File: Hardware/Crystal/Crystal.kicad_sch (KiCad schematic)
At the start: 48 parts, among them J1 USB_B_Micro, U1 AP63205WU, U2 NCP1117-3.3_SOT223, U3 ESP32-C3-WROOM-02, U4 TXS0102DCT, U5 TXS0108EPW

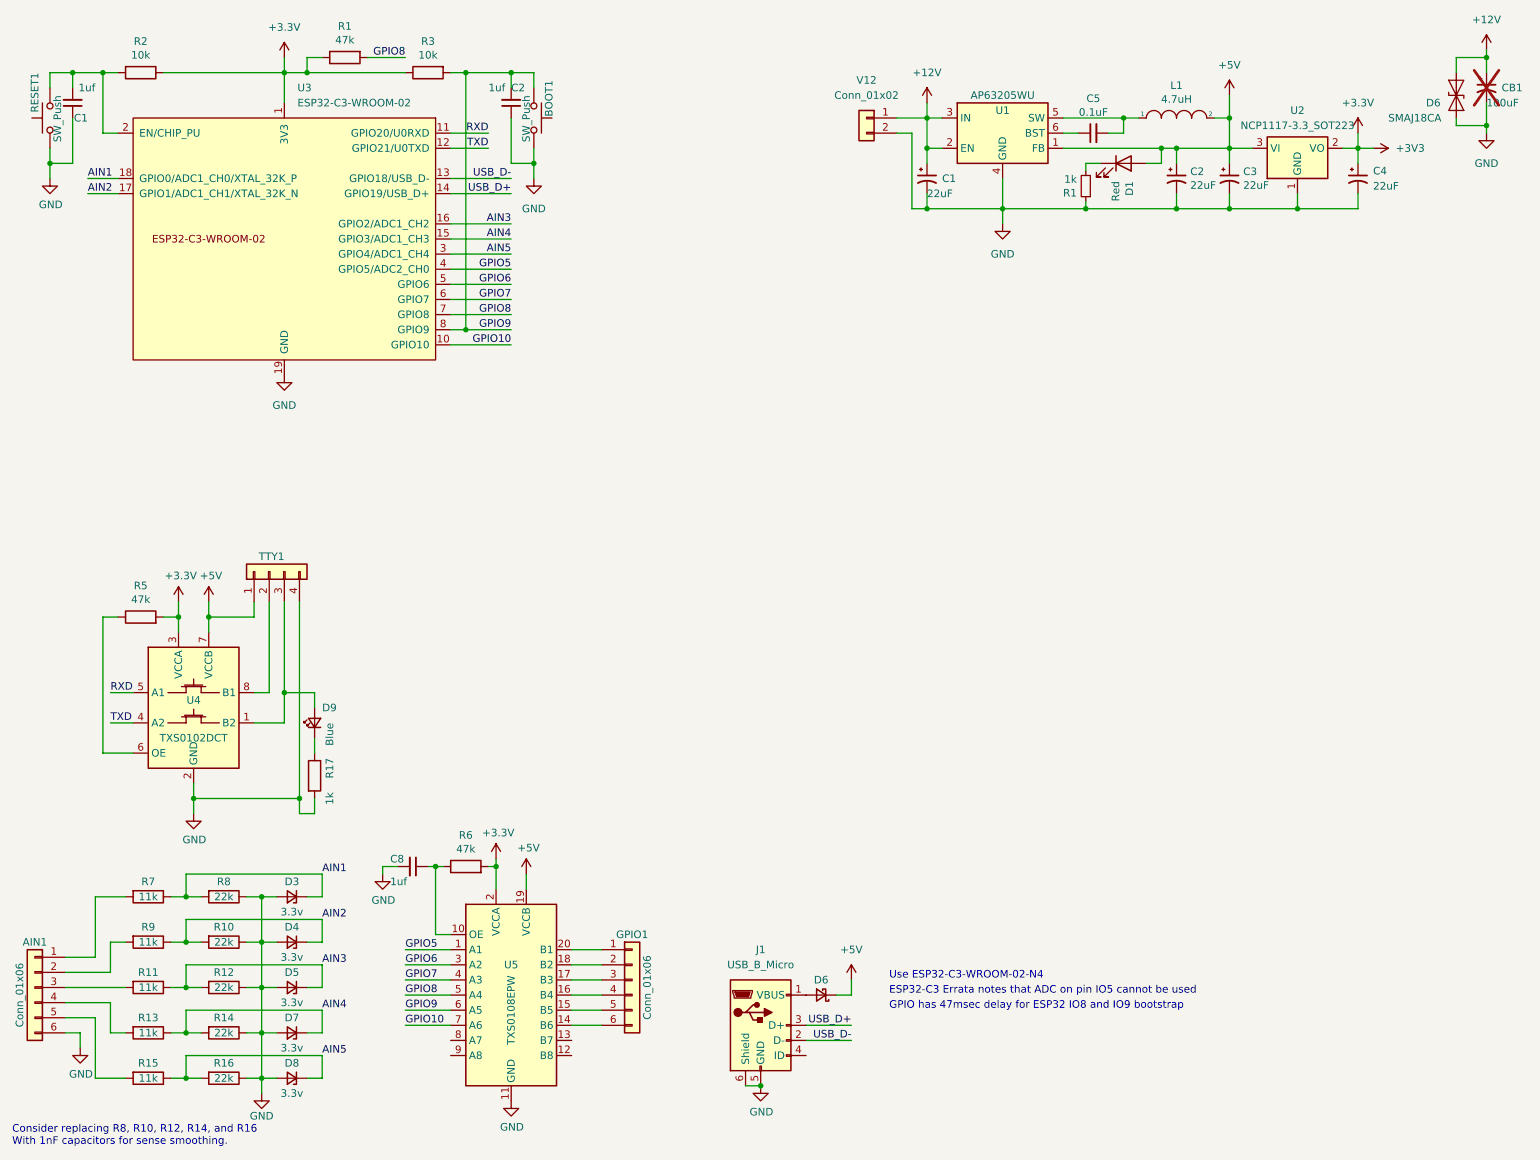
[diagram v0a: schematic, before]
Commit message: Further PCB revision to use MLCC caps in the 5v regulator for better smoothing and space utilization
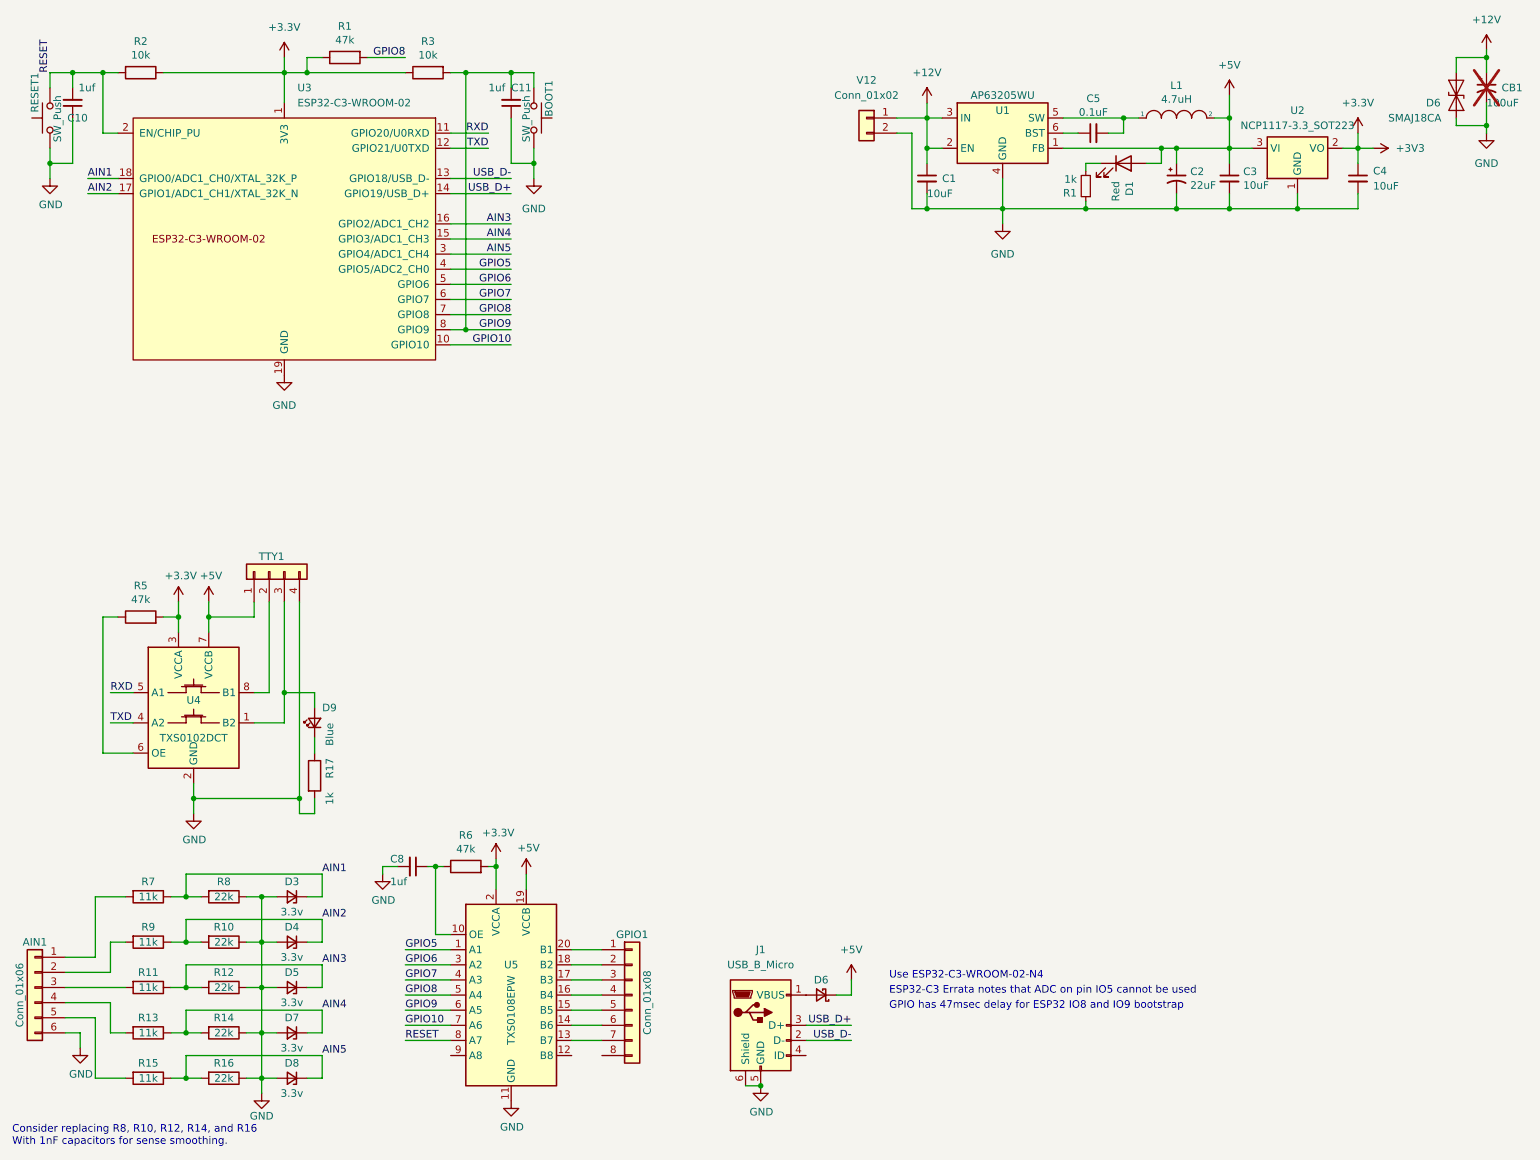
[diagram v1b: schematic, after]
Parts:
- C1, C3: value 22uF -> 10uF; footprint Capacitor_SMD:CP_Elec_5x5.3 -> Capacitor_SMD:C_1210_3225Metric; symbol Motor Shield Adapter-rescue:CP1_Small-Device -> Device:C_Small; LCSC SKU C2164091 -> C2175202; MFG Wurth Electronik -> Murata; PN 865080542006 -> GRT31CR6YA106ME01L
- C4: value 22uF -> 10uF; footprint Capacitor_SMD:CP_Elec_5x5.3 -> Capacitor_SMD:C_1210_3225Metric; symbol Device:C_Polarized_Small_US -> Device:C_Small; LCSC SKU C2164091 -> C2175202; MFG Wurth Electronik -> Murata; PN 865080542006 -> GRT31CR6YA106ME01L
- GPIO1: value Conn_01x06 -> Conn_01x08; footprint Connector_PinSocket_2.54mm:PinSocket_1x06_P2.54mm_Vertical -> Connector_PinSocket_2.54mm:PinSocket_1x08_P2.54mm_Vertical; symbol Connector_Generic:Conn_01x06 -> Connector_Generic:Conn_01x08; PN 929850-01-06-RA -> 929850-01-08-RA
- renumbered C1 to C10, C2 to C11
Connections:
- net at U5.13 (B7): now also GPIO1.7 (Pin_7)
- net RESET: now reaches U5.8 (A7)
- net RESET: now also C10.2, R2.2, RESET1.2, U3.2 (EN/CHIP_PU)
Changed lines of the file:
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@@
   (title_block
     (title "Crystal - ESP32-C3 wifi adapter")
-    (date "2023-12-30")
-    (rev "0.6")
+    (date "2024-01-12")
+    (rev "0.8")
     (company "SeraphimLabs LLC")
   )
@@
     (stroke (width 0) (type default))
   )
+  (wire (pts (xy 78.74 185.42) (xy 86.36 185.42))
+    (stroke (width 0) (type default))
+  )
   (wire (pts (xy 208.28 43.18) (xy 208.28 45.72))
     (stroke (width 0) (type default))
@@
   )
   (wire (pts (xy 106.68 175.26) (xy 111.76 175.26))
+    (stroke (width 0) (type default))
+  )
+  (wire (pts (xy 106.68 185.42) (xy 111.76 185.42))
     (stroke (width 0) (type default))
   )
@@
     (effects (font (size 1.27 1.27)) (justify right bottom))
   )
+  (label "RESET" (at 19.05 22.86 90) (fields_autoplaced)
+    (effects (font (size 1.27 1.27)) (justify left bottom))
+  )
   (label "AIN4" (at 64.77 180.34 0) (fields_autoplaced)
     (effects (font (size 1.27 1.27)) (justify left bottom))
@@
   )
   (label "AIN2" (at 64.77 165.1 0) (fields_autoplaced)
+    (effects (font (size 1.27 1.27)) (justify left bottom))
+  )
+  (label "RESET" (at 78.74 185.42 0) (fields_autoplaced)
     (effects (font (size 1.27 1.27)) (justify left bottom))
   )
@@
   (symbol (lib_id "Device:C_Small") (at 22.86 27.94 180) (unit 1)
     (in_bom yes) (on_board yes) (dnp no)
-    (property "Reference" "C1" (at 25.4 30.48 0)
+    (property "Reference" "C10" (at 25.4 30.48 0)
       (effects (font (size 1.27 1.27)) (justify left))
     )
@@
       (project "Crystal"
         (path "/dd8844b3-8da5-475e-be7b-df38aec3ae9d"
-          (reference "C1") (unit 1)
+          (reference "C10") (unit 1)
         )
       )
@@
     )
   )
-  (symbol (lib_id "Motor Shield Adapter-rescue:CP1_Small-Device") (at 166.37 40.64 0) (unit 1)
+  (symbol (lib_id "Device:C_Small") (at 166.37 40.64 0) (unit 1)
     (in_bom yes) (on_board yes) (dnp no)
     (property "Reference" "C1" (at 168.91 40.64 0)
       (effects (font (size 1.27 1.27)) (justify left))
     )
-    (property "Value" "22uF" (at 166.37 43.18 0)
+    (property "Value" "10uF" (at 166.37 43.18 0)
       (effects (font (size 1.27 1.27)) (justify left))
     )
-    (property "Footprint" "Capacitor_SMD:CP_Elec_5x5.3" (at 166.37 40.64 0)
+    (property "Footprint" "Capacitor_SMD:C_1210_3225Metric" (at 166.37 40.64 0)
       (effects (font (size 1.27 1.27)) hide)
     )
@@
       (effects (font (size 1.27 1.27)) hide)
     )
-    (property "MFG" "Wurth Electronik" (at 166.37 40.64 0)
-      (effects (font (size 1.27 1.27)) hide)
-    )
-    (property "PN" "865080542006" (at 166.37 40.64 0)
-      (effects (font (size 1.27 1.27)) hide)
-    )
-    (property "LCSC SKU" "C2164091" (at 166.37 40.64 0)
+    (property "MFG" "Murata" (at 166.37 40.64 0)
+      (effects (font (size 1.27 1.27)) hide)
+    )
+    (property "PN" "GRT31CR6YA106ME01L" (at 166.37 40.64 0)
+      (effects (font (size 1.27 1.27)) hide)
+    )
+    (property "LCSC SKU" "C2175202" (at 166.37 40.64 0)
       (effects (font (size 1.27 1.27)) hide)
     )
@@
       (project "Crystal"
         (path "/dd8844b3-8da5-475e-be7b-df38aec3ae9d"
-          (reference "C4") (unit 1)
+          (reference "C1") (unit 1)
         )
       )
@@
       (project "Crystal"
         (path "/dd8844b3-8da5-475e-be7b-df38aec3ae9d"
-          (reference "C5") (unit 1)
+          (reference "C2") (unit 1)
         )
       )
@@
     )
   )
-  (symbol (lib_id "Motor Shield Adapter-rescue:CP1_Small-Device") (at 217.17 40.64 0) (unit 1)
+  (symbol (lib_id "Device:C_Small") (at 217.17 40.64 0) (unit 1)
     (in_bom yes) (on_board yes) (dnp no)
     (property "Reference" "C3" (at 219.4814 39.4716 0)
       (effects (font (size 1.27 1.27)) (justify left))
     )
-    (property "Value" "22uF" (at 219.4814 41.783 0)
+    (property "Value" "10uF" (at 219.4814 41.783 0)
       (effects (font (size 1.27 1.27)) (justify left))
     )
-    (property "Footprint" "Capacitor_SMD:CP_Elec_5x5.3" (at 217.17 40.64 0)
+    (property "Footprint" "Capacitor_SMD:C_1210_3225Metric" (at 217.17 40.64 0)
       (effects (font (size 1.27 1.27)) hide)
     )
@@
       (effects (font (size 1.27 1.27)) hide)
     )
-    (property "MFG" "Wurth Electronik" (at 217.17 40.64 0)
-      (effects (font (size 1.27 1.27)) hide)
-    )
-    (property "PN" "865080542006" (at 217.17 40.64 0)
-      (effects (font (size 1.27 1.27)) hide)
-    )
-    (property "LCSC SKU" "C2164091" (at 217.17 40.64 0)
+    (property "MFG" "Murata" (at 217.17 40.64 0)
+      (effects (font (size 1.27 1.27)) hide)
+    )
+    (property "PN" "GRT31CR6YA106ME01L" (at 217.17 40.64 0)
+      (effects (font (size 1.27 1.27)) hide)
+    )
+    (property "LCSC SKU" "C2175202" (at 217.17 40.64 0)
       (effects (font (size 1.27 1.27)) hide)
     )
@@
       (project "Crystal"
         (path "/dd8844b3-8da5-475e-be7b-df38aec3ae9d"
-          (reference "C6") (unit 1)
+          (reference "C4") (unit 1)
         )
       )
@@
     )
   )
-  (symbol (lib_id "Connector_Generic:Conn_01x06") (at 116.84 175.26 0) (unit 1)
+  (symbol (lib_id "Connector_Generic:Conn_01x08") (at 116.84 177.8 0) (unit 1)
     (in_bom yes) (on_board yes) (dnp no)
     (property "Reference" "GPIO1" (at 116.84 167.64 0)
       (effects (font (size 1.27 1.27)))
     )
-    (property "Value" "Conn_01x06" (at 119.38 176.53 90)
-      (effects (font (size 1.27 1.27)))
-    )
-    (property "Footprint" "Connector_PinSocket_2.54mm:PinSocket_1x06_P2.54mm_Vertical" (at 116.84 175.26 0)
-      (effects (font (size 1.27 1.27)) hide)
-    )
-    (property "Datasheet" "~" (at 116.84 175.26 0)
-      (effects (font (size 1.27 1.27)) hide)
-    )
-    (property "MFG" "3M" (at 116.84 175.26 0)
-      (effects (font (size 1.27 1.27)) hide)
-    )
-    (property "PN" "929850-01-06-RA" (at 116.84 175.26 0)
-      (effects (font (size 1.27 1.27)) hide)
-    )
-    (property "LCSC SKU" "" (at 116.84 175.26 0)
+    (property "Value" "Conn_01x08" (at 119.38 179.07 90)
+      (effects (font (size 1.27 1.27)))
+    )
+    (property "Footprint" "Connector_PinSocket_2.54mm:PinSocket_1x08_P2.54mm_Vertical" (at 116.84 177.8 0)
+      (effects (font (size 1.27 1.27)) hide)
+    )
+    (property "Datasheet" "~" (at 116.84 177.8 0)
+      (effects (font (size 1.27 1.27)) hide)
+    )
+    (property "MFG" "3M" (at 116.84 177.8 0)
+      (effects (font (size 1.27 1.27)) hide)
+    )
+    (property "PN" "929850-01-08-RA" (at 116.84 177.8 0)
+      (effects (font (size 1.27 1.27)) hide)
+    )
+    (property "LCSC SKU" "" (at 116.84 177.8 0)
       (effects (font (size 1.27 1.27)) hide)
     )
@@
     (pin "5")
     (pin "6")
+    (pin "7")
+    (pin "8")
     (instances
       (project "Crystal"
@@
     )
   )
-  (symbol (lib_id "Device:C_Polarized_Small_US") (at 238.76 40.64 0) (unit 1)
+  (symbol (lib_id "Device:C_Small") (at 238.76 40.64 0) (unit 1)
     (in_bom yes) (on_board yes) (dnp no)
     (property "Reference" "C4" (at 241.3 39.37 0)
       (effects (font (size 1.27 1.27)) (justify left))
     )
-    (property "Value" "22uF" (at 241.3 41.91 0)
+    (property "Value" "10uF" (at 241.3 41.91 0)
       (effects (font (size 1.27 1.27)) (justify left))
     )
-    (property "Footprint" "Capacitor_SMD:CP_Elec_5x5.3" (at 238.76 40.64 0)
+    (property "Footprint" "Capacitor_SMD:C_1210_3225Metric" (at 238.76 40.64 0)
       (effects (font (size 1.27 1.27)) hide)
     )
@@
       (effects (font (size 1.27 1.27)) hide)
     )
-    (property "MFG" "Wurth Electronik" (at 238.76 40.64 0)
-      (effects (font (size 1.27 1.27)) hide)
-    )
-    (property "PN" "865080542006" (at 238.76 40.64 0)
-      (effects (font (size 1.27 1.27)) hide)
-    )
-    (property "LCSC SKU" "C2164091" (at 238.76 40.64 0)
+    (property "MFG" "Murata" (at 238.76 40.64 0)
+      (effects (font (size 1.27 1.27)) hide)
+    )
+    (property "PN" "GRT31CR6YA106ME01L" (at 238.76 40.64 0)
+      (effects (font (size 1.27 1.27)) hide)
+    )
+    (property "LCSC SKU" "C2175202" (at 238.76 40.64 0)
       (effects (font (size 1.27 1.27)) hide)
     )
@@
       (project "Crystal"
         (path "/dd8844b3-8da5-475e-be7b-df38aec3ae9d"
-          (reference "C7") (unit 1)
+          (reference "C5") (unit 1)
         )
       )
@@
   (symbol (lib_id "Device:C_Small") (at 96.52 27.94 0) (mirror x) (unit 1)
     (in_bom yes) (on_board yes) (dnp no)
-    (property "Reference" "C2" (at 96.52 25.4 0)
+    (property "Reference" "C11" (at 96.52 25.4 0)
       (effects (font (size 1.27 1.27)) (justify left))
     )
@@
       (project "Crystal"
         (path "/dd8844b3-8da5-475e-be7b-df38aec3ae9d"
-          (reference "C2") (unit 1)
-        )
-      )
+          (reference "C11") (unit 1)
+        )
+      )
